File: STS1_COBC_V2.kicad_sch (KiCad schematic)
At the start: 14 parts, among them U1 coordinate_system

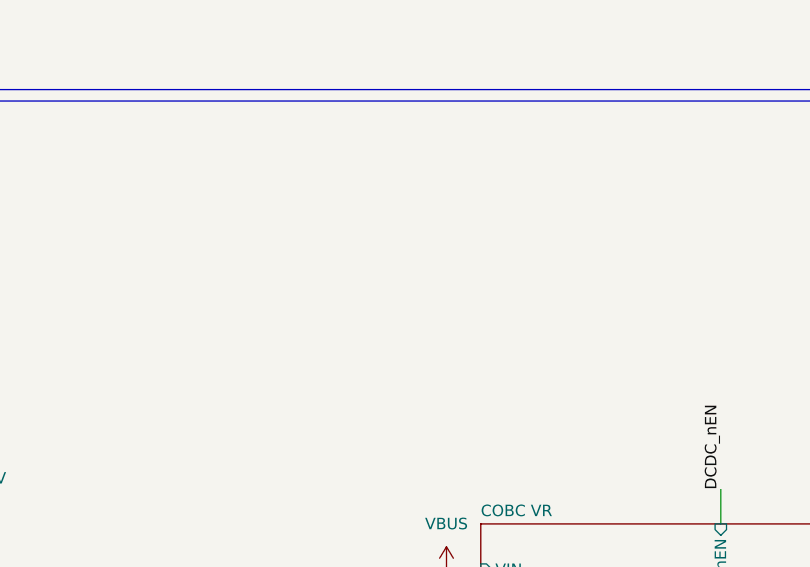
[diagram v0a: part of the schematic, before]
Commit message: Add resetdog timer (RDT) schematics
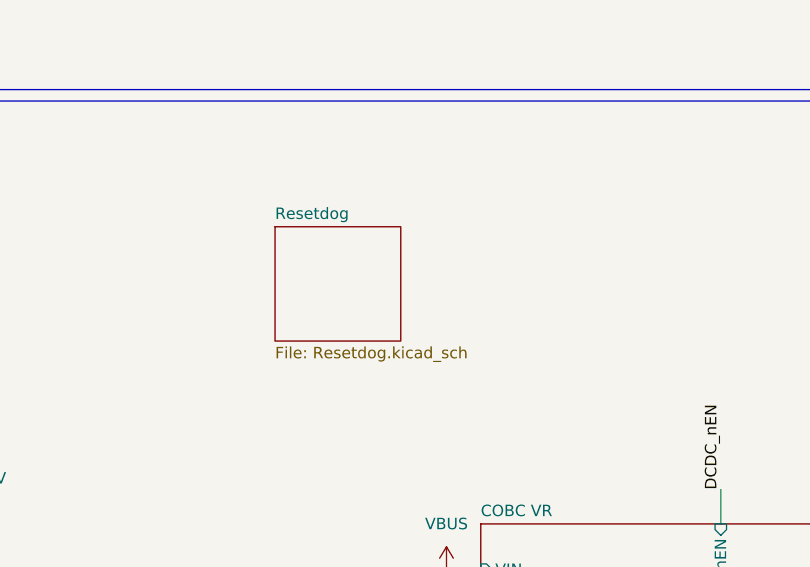
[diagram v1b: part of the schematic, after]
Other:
- added sheet Resetdog (Resetdog.kicad_sch)
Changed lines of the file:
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@@
+    )
+  )
+  (sheet (at 95.25 115.57) (size 13.97 12.7) (fields_autoplaced)
+    (stroke (width 0.1524) (type solid) (color 0 0 0 0))
+    (fill (color 0 0 0 0.0000))
+    (property "Sheet name" "Resetdog" (id 0) (at 95.25 114.8584 0)
+      (effects (font (size 1.27 1.27)) (justify left bottom))
+    )
+    (property "Sheet file" "Resetdog.kicad_sch" (id 1) (at 95.25 128.8546 0)
+      (effects (font (size 1.27 1.27)) (justify left top))
     )
   )
@@
     (path "/a8678e8a-595e-4c52-9d87-4220609965c5" (page "8"))
     (path "/a8678e8a-595e-4c52-9d87-4220609965c5/5020136b-5eea-4a2f-9bc4-470d670f3f42" (page "9"))
+    (path "/f6bcd7c0-6cce-4fe3-9b39-774a553787dc" (page "9"))
     (path "/00000000-0000-0000-0000-000059c45183" (page "#"))
   )
@@
       (reference "#PWR0193") (unit 1) (value "VBUS") (footprint "")
     )
+    (path "/f6bcd7c0-6cce-4fe3-9b39-774a553787dc/2114c7a2-319e-4aff-bd16-4cee0ff4d1e9"
+      (reference "#PWR?") (unit 1) (value "+3V3") (footprint "")
+    )
+    (path "/f6bcd7c0-6cce-4fe3-9b39-774a553787dc/3fba0d24-c78e-4942-8aaf-8452d6d54d7f"
+      (reference "#PWR?") (unit 1) (value "+3V3") (footprint "")
+    )
+    (path "/f6bcd7c0-6cce-4fe3-9b39-774a553787dc/479ad715-dc5f-448b-8992-368e3c72418b"
+      (reference "#PWR?") (unit 1) (value "GND") (footprint "")
+    )
+    (path "/f6bcd7c0-6cce-4fe3-9b39-774a553787dc/58a8ee2a-cc0d-4b59-8094-4d6af312770f"
+      (reference "#PWR?") (unit 1) (value "GND") (footprint "")
+    )
+    (path "/f6bcd7c0-6cce-4fe3-9b39-774a553787dc/6bdc5ca0-01c4-4cef-ae75-d366e2549c42"
+      (reference "#PWR?") (unit 1) (value "GND") (footprint "")
+    )
+    (path "/f6bcd7c0-6cce-4fe3-9b39-774a553787dc/6f101025-a762-41b7-99fa-91fef04d9293"
+      (reference "#PWR?") (unit 1) (value "+3V3") (footprint "")
+    )
+    (path "/f6bcd7c0-6cce-4fe3-9b39-774a553787dc/72b9ac34-1eaa-48ad-9d49-1710e8901ce0"
+      (reference "#PWR?") (unit 1) (value "GND") (footprint "")
+    )
+    (path "/f6bcd7c0-6cce-4fe3-9b39-774a553787dc/882379e8-10a0-47e9-82b7-4954b719058b"
+      (reference "#PWR?") (unit 1) (value "GND") (footprint "")
+    )
+    (path "/f6bcd7c0-6cce-4fe3-9b39-774a553787dc/a0d2f398-b757-4728-90c2-6bf071bacaf1"
+      (reference "#PWR?") (unit 1) (value "+3V3") (footprint "")
+    )
+    (path "/f6bcd7c0-6cce-4fe3-9b39-774a553787dc/c020c9cf-8289-4144-b4be-707c5841673c"
+      (reference "#PWR?") (unit 1) (value "GND") (footprint "")
+    )
+    (path "/f6bcd7c0-6cce-4fe3-9b39-774a553787dc/da062ca1-36d7-422b-b054-c34dfc0e1028"
+      (reference "#PWR?") (unit 1) (value "GND") (footprint "")
+    )
+    (path "/f6bcd7c0-6cce-4fe3-9b39-774a553787dc/efaea70a-5329-4cd8-9660-febcbb47a9a2"
+      (reference "#PWR?") (unit 1) (value "+3V3") (footprint "")
+    )
+    (path "/f6bcd7c0-6cce-4fe3-9b39-774a553787dc/ffbe8ff4-029b-4baa-8a5d-2175d5119d2b"
+      (reference "#PWR?") (unit 1) (value "GND") (footprint "")
+    )
     (path "/a8678e8a-595e-4c52-9d87-4220609965c5/00000000-0000-0000-0000-0000612dbaa7"
       (reference "C1") (unit 1) (value "100n") (footprint "Capacitor_SMD:C_0805_2012Metric")
@@
       (reference "C79") (unit 1) (value "100nF") (footprint "Capacitor_SMD:C_0603_1608Metric")
     )
+    (path "/f6bcd7c0-6cce-4fe3-9b39-774a553787dc/504e1d76-1315-46f2-a027-ace7857f4f41"
+      (reference "C?") (unit 1) (value "1u") (footprint "Capacitor_SMD:C_0603_1608Metric")
+    )
+    (path "/f6bcd7c0-6cce-4fe3-9b39-774a553787dc/d566c052-999c-4d8e-b62d-dd58e45a690b"
+      (reference "C?") (unit 1) (value "4.7u") (footprint "Capacitor_SMD:C_0603_1608Metric")
+    )
+    (path "/f6bcd7c0-6cce-4fe3-9b39-774a553787dc/d8da4bb3-f0cd-4caa-ac9c-b71bbf6d2614"
+      (reference "C?") (unit 1) (value "1u") (footprint "Capacitor_SMD:C_0603_1608Metric")
+    )
     (path "/00000000-0000-0000-0000-000059c45183/00000000-0000-0000-0000-00006179b797"
       (reference "CSBI_1") (unit 1) (value "~") (footprint "Connector_PinSocket_2.00mm:PinSocket_2x25_P2.00mm_Vertical")
@@
       (reference "D8") (unit 1) (value "LED") (footprint "LED_SMD:LED_0805_2012Metric")
     )
+    (path "/f6bcd7c0-6cce-4fe3-9b39-774a553787dc/8422e768-fe2b-43fa-87fd-771b6f4b8af2"
+      (reference "D?") (unit 1) (value "BAS70H") (footprint "Diode_SMD:D_SOD-323")
+    )
     (path "/a8678e8a-595e-4c52-9d87-4220609965c5/5020136b-5eea-4a2f-9bc4-470d670f3f42/ee13059c-4243-43cc-a1cb-962be7eb3ace"
       (reference "FB1") (unit 1) (value "Ferrite_Bead") (footprint "Inductor_SMD:L_0603_1608Metric")
@@
       (reference "JP1") (unit 1) (value "SolderJumper_2_Open") (footprint "Jumper:SolderJumper-2_P1.3mm_Open_TrianglePad1.0x1.5mm")
     )
+    (path "/f6bcd7c0-6cce-4fe3-9b39-774a553787dc/fdb9af79-ab4a-4a50-a349-00dcf3e3d6f1"
+      (reference "JP?") (unit 1) (value "~{RDT}") (footprint "Jumper:SolderJumper-2_P1.3mm_Open_Pad1.0x1.5mm")
+    )
     (path "/a8678e8a-595e-4c52-9d87-4220609965c5/80af458f-c7a5-433b-9df7-795777bcc769"
       (reference "L1") (unit 1) (value "15n") (footprint "Inductor_SMD:L_0402_1005Metric")
@@
       (reference "R35") (unit 1) (value "220R") (footprint "Resistor_SMD:R_0603_1608Metric")
     )
+    (path "/f6bcd7c0-6cce-4fe3-9b39-774a553787dc/17cafd9e-ac79-419a-af90-236b2a8e3605"
+      (reference "R?") (unit 1) (value "220K") (footprint "Resistor_SMD:R_0603_1608Metric")
+    )
+    (path "/f6bcd7c0-6cce-4fe3-9b39-774a553787dc/64a74366-b203-497d-8a0f-b1030fb18217"
+      (reference "R?") (unit 1) (value "4.7M") (footprint "Resistor_SMD:R_0603_1608Metric")
+    )
+    (path "/f6bcd7c0-6cce-4fe3-9b39-774a553787dc/9b5be1c9-cca2-4494-bf00-b8727032d52f"
+      (reference "R?") (unit 1) (value "1k") (footprint "Resistor_SMD:R_0603_1608Metric")
+    )
+    (path "/f6bcd7c0-6cce-4fe3-9b39-774a553787dc/e003bc87-c461-459a-a1aa-69bf223aeb47"
+      (reference "R?") (unit 1) (value "2.2M") (footprint "Resistor_SMD:R_0603_1608Metric")
+    )
     (path "/a8678e8a-595e-4c52-9d87-4220609965c5/00000000-0000-0000-0000-000061b6aef9"
       (reference "TP1") (unit 1) (value "SiVCC") (footprint "STS1library:STS1_Testpoint")
@@
       (reference "U13") (unit 1) (value "TQP7M9106") (footprint "Package_DFN_QFN:QFN-24-1EP_4x4mm_P0.5mm_EP2.7x2.7mm_ThermalVias")
     )
+    (path "/f6bcd7c0-6cce-4fe3-9b39-774a553787dc/3a34c2b8-75af-4c84-8e63-5de5e175ee76"
+      (reference "U?") (unit 1) (value "MC74HC4538ADG") (footprint "SOIC127P600X175-16N")
+    )
+    (path "/f6bcd7c0-6cce-4fe3-9b39-774a553787dc/93ec6816-cd04-45c6-9b19-211999d714a0"
+      (reference "U?") (unit 1) (value "MC14541BD") (footprint "Package_SO:SOIC-14_3.9x8.7mm_P1.27mm")
+    )
     (path "/be3cc363-80eb-4df5-9a1b-912085b5cf84/00000000-0000-0000-0000-00006254c1e3"

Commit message: Add preliminary resetdog PCB layout.
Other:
- sheet COBC STM ports: added RDT_CLR; removed DCDC_nEN
- sheet Resetdog ports: added DCDC_nEN, RDT_CLR; removed none

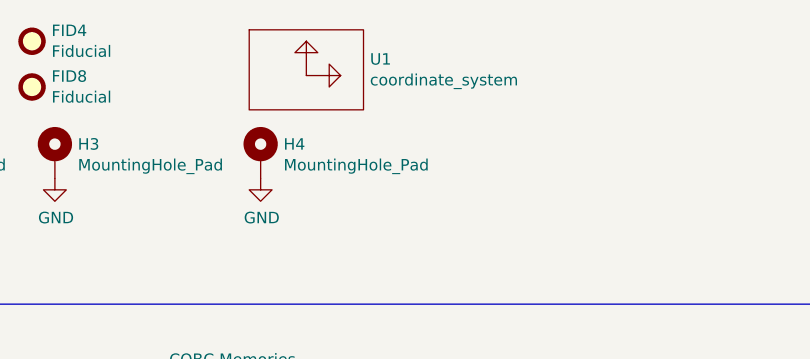
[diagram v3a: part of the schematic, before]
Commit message: Rotate coordinate system (x,y,z)->(y,-x,z)
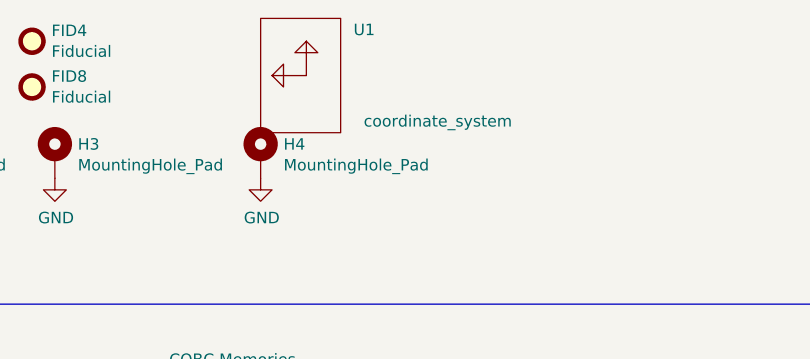
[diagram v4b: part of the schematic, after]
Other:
- moved on the sheet: U1
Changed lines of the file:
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@@
     (pin "1")
   )
-  (symbol (lib_id "STS-connector:coordinate_system") (at 92.71 19.05 0) (unit 1)
+  (symbol (lib_id "STS-connector:coordinate_system") (at 92.71 19.05 90) (unit 1)
     (in_bom yes) (on_board yes)
-    (property "Reference" "U1" (id 0) (at 99.7712 17.2466 0)
+    (property "Reference" "U1" (id 0) (at 100.33 13.97 90)
       (effects (font (size 1.27 1.27)) (justify left))
     )
-    (property "Value" "coordinate_system" (id 1) (at 99.7712 19.558 0)
+    (property "Value" "coordinate_system" (id 1) (at 115.57 24.13 90)
       (effects (font (size 1.27 1.27)) (justify left))
     )
